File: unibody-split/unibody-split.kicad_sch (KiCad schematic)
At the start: 93 parts, among them IC1 AP130-20, SW1 SW_Push, SW10 SW_Push, SW11 SW_Push, SW12 SW_Push, SW13 SW_Push, SW14 SW_Push, SW15 SW_Push, SW16 SW_Push, SW17 SW_Push, SW18 SW_Push, SW19 SW_Push, SW2 SW_Push, SW20 SW_Push, SW21 SW_Push, SW22 SW_Push, SW23 SW_Push, SW24 SW_Push, SW25 SW_Push, SW26 SW_Push, SW27 SW_Push, SW28 SW_Push, SW29 SW_Push, SW3 SW_Push, SW30 SW_Push, SW31 SW_Push, SW32 SW_Push, SW33 SW_Push, SW34 SW_Push, SW35 SW_Push, SW36 SW_Push, SW37 SW_Push, SW38 SW_Push, SW39 SW_Push, SW4 SW_Push, SW40 SW_Push, SW41 SW_Push, SW42 SW_Push, SW5 SW_Push, SW6 SW_Push, SW7 SW_Push, SW8 SW_Push, SW9 SW_Push, U1 Pico, U2 PMW3360DM-T2QU

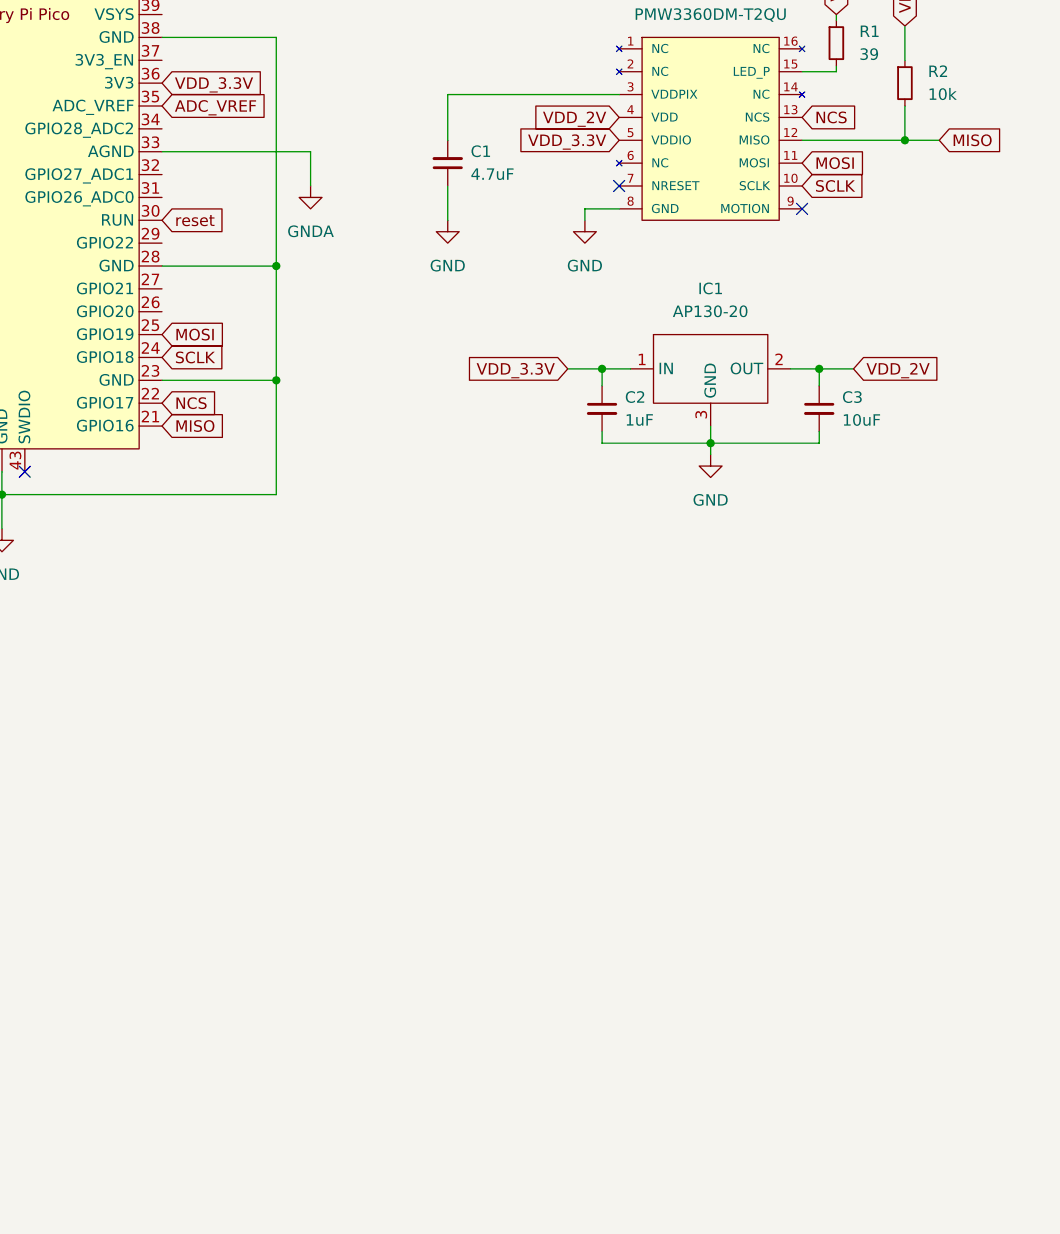
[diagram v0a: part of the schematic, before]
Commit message: Add joystick to schematics
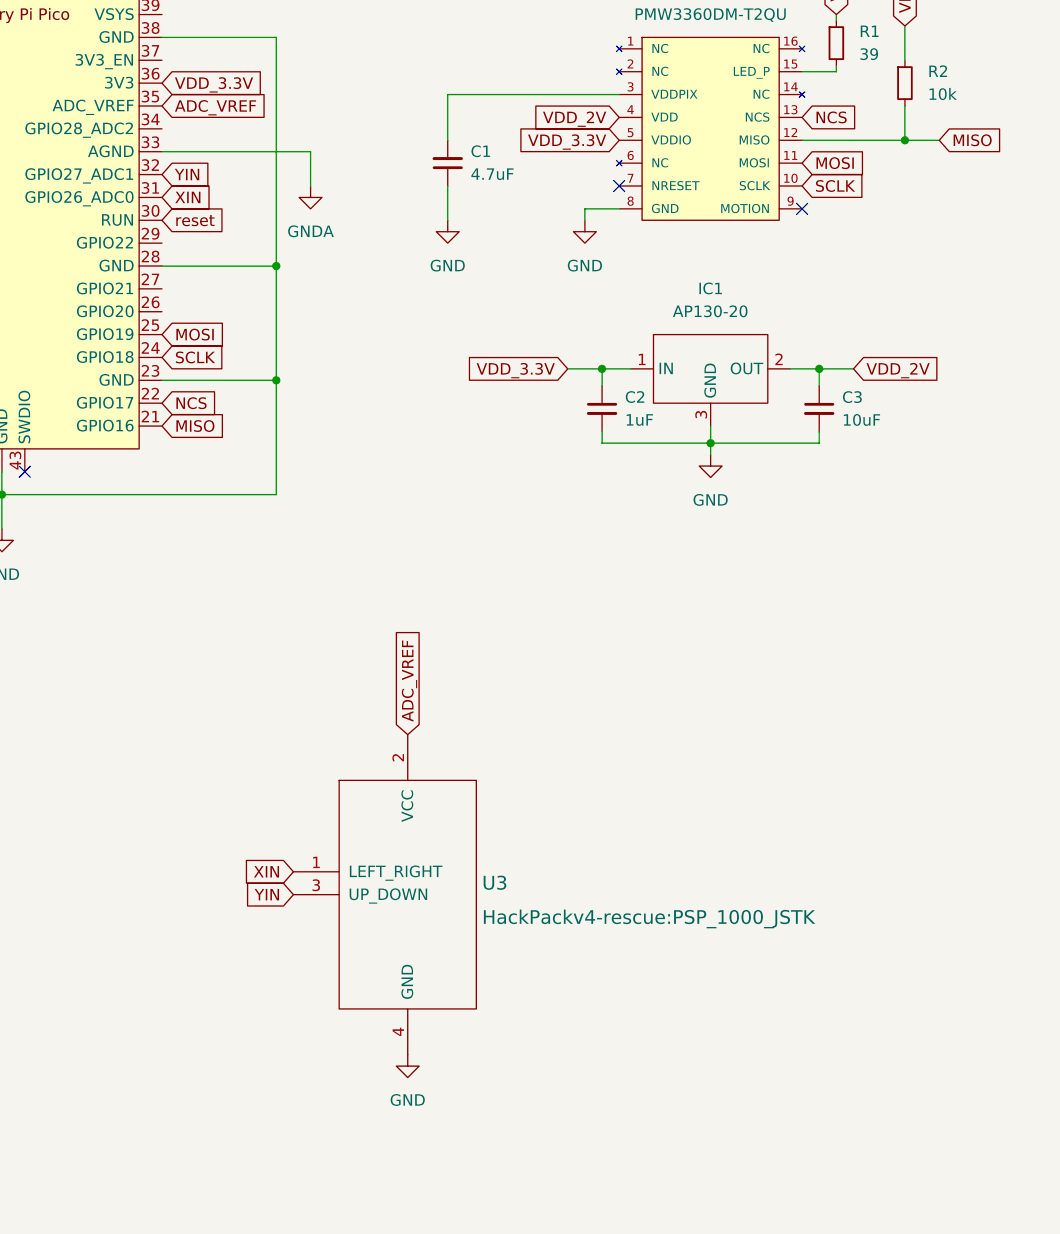
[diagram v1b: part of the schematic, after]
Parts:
- added U3: HackPackv4-rescue:PSP_1000_JSTK, HackPack_Footprints:JOYSTICK-PSP1000, symbol HackPackv4-cache:HackPackv4-rescue{colon}PSP_1000_JSTK
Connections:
- net ADC_VREF: now also U3.2 (VCC)
- net GND: now also U3.4 (GND)
- net XIN: now reaches U1.31 (GPIO26_ADC0)
- net XIN: now also U3.1 (LEFT_RIGHT)
- net YIN: now reaches U1.32 (GPIO27_ADC1)
- net YIN: now also U3.3 (UP_DOWN)
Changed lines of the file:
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@@
+    )
+  )
+  (global_label "XIN" (shape input) (at 75.565 121.92 180) (fields_autoplaced)
+    (effects (font (size 1.27 1.27)) (justify right))
+    (property "Intersheet References" "${INTERSHEET_REFS}" (id 0) (at 70.0071 121.8406 0)
+      (effects (font (size 1.27 1.27)) (justify right) hide)
     )
   )
@@
     )
   )
+  (global_label "XIN" (shape input) (at 60.96 46.99 0) (fields_autoplaced)
+    (effects (font (size 1.27 1.27)) (justify left))
+    (property "Intersheet References" "${INTERSHEET_REFS}" (id 0) (at 66.5179 47.0694 0)
+      (effects (font (size 1.27 1.27)) (justify left) hide)
+    )
+  )
   (global_label "col4" (shape input) (at 25.4 36.83 180) (fields_autoplaced)
     (effects (font (size 1.27 1.27)) (justify right))
@@
     )
   )
+  (global_label "ADC_VREF" (shape input) (at 88.265 106.68 90) (fields_autoplaced)
+    (effects (font (size 1.27 1.27)) (justify left))
+    (property "Intersheet References" "${INTERSHEET_REFS}" (id 0) (at 88.1856 95.0745 90)
+      (effects (font (size 1.27 1.27)) (justify left) hide)
+    )
+  )
   (global_label "row4" (shape input) (at 172.72 109.855 180) (fields_autoplaced)
     (effects (font (size 1.27 1.27)) (justify right))
@@
     )
   )
+  (global_label "YIN" (shape input) (at 75.565 124.46 180) (fields_autoplaced)
+    (effects (font (size 1.27 1.27)) (justify right))
+    (property "Intersheet References" "${INTERSHEET_REFS}" (id 0) (at 70.1281 124.3806 0)
+      (effects (font (size 1.27 1.27)) (justify right) hide)
+    )
+  )
   (global_label "VDD_3.3V" (shape input) (at 106.045 66.04 180) (fields_autoplaced)
     (effects (font (size 1.27 1.27)) (justify right))
@@
     )
   )
+  (global_label "YIN" (shape input) (at 60.96 44.45 0) (fields_autoplaced)
+    (effects (font (size 1.27 1.27)) (justify left))
+    (property "Intersheet References" "${INTERSHEET_REFS}" (id 0) (at 66.3969 44.5294 0)
+      (effects (font (size 1.27 1.27)) (justify left) hide)
+    )
+  )
   (symbol (lib_id "Diode:1N4148") (at 203.835 106.045 90) (unit 1)
     (in_bom yes) (on_board yes)
@@
     (pin "1")
     (pin "2")
+  )
+  (symbol (lib_id "HackPackv4-cache:HackPackv4-rescue{colon}PSP_1000_JSTK") (at 88.265 123.19 0) (unit 1)
+    (in_bom yes) (on_board yes) (fields_autoplaced)
+    (property "Reference" "U3" (id 0) (at 96.52 123.19 0)
+      (effects (font (size 1.524 1.524)) (justify left))
+    )
+    (property "Value" "HackPackv4-rescue:PSP_1000_JSTK" (id 1) (at 96.52 127 0)
+      (effects (font (size 1.524 1.524)) (justify left))
+    )
+    (property "Footprint" "HackPack_Footprints:JOYSTICK-PSP1000" (id 2) (at 121.285 140.97 0)
+      (effects (font (size 1.524 1.524)) hide)
+    )
+    (property "Datasheet" "" (id 3) (at 121.285 140.97 0)
+      (effects (font (size 1.524 1.524)) hide)
+    )
+    (pin "1")
+    (pin "2")
+    (pin "3")
+    (pin "4")
   )
   (symbol (lib_id "Switch:SW_Push") (at 181.61 102.235 0) (unit 1)
@@
     (pin "2")
   )
+  (symbol (lib_id "power:GND") (at 88.265 142.24 0) (unit 1)
+    (in_bom yes) (on_board yes) (fields_autoplaced)
+    (property "Reference" "#PWR06" (id 0) (at 88.265 148.59 0)
+      (effects (font (size 1.27 1.27)) hide)
+    )
+    (property "Value" "GND" (id 1) (at 88.265 147.32 0))
+    (property "Footprint" "" (id 2) (at 88.265 142.24 0)
+      (effects (font (size 1.27 1.27)) hide)
+    )
+    (property "Datasheet" "" (id 3) (at 88.265 142.24 0)
+      (effects (font (size 1.27 1.27)) hide)
+    )
+    (pin "1")
+  )
   (symbol (lib_id "Diode:1N4148") (at 220.98 88.265 90) (unit 1)
     (in_bom yes) (on_board yes) (fields_autoplaced)
@@
       (reference "#PWR05") (unit 1) (value "GND") (footprint "")
     )
+    (path "/6ee8ed8a-f9e3-49c8-9ed2-6cebe4a20089"
+      (reference "#PWR06") (unit 1) (value "GND") (footprint "")
+    )
     (path "/41d2141b-2555-41d1-9b61-56c4033530d3"
       (reference "#PWR07") (unit 1) (value "GND") (footprint "")
@@
       (reference "U2") (unit 1) (value "PMW3360DM-T2QU") (footprint "local:DIP-16_W10.16mm")
     )
-  )
+    (path "/1928514b-b204-4adc-b538-8b1b61c3f64e"
+      (reference "U3") (unit 1) (value "HackPackv4-rescue:PSP_1000_JSTK") (footprint "HackPack_Footprints:JOYSTICK-PSP1000")
+    )
+  )
